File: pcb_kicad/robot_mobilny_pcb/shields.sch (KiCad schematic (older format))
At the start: 9 parts, among them J10 LIDAR, J11 MOTOR_1&2, J12 ENCODER_MOT_2, J13 ENCODER_MOT_3, J14 MOTOR_3&4, J15 ENCODER_MOT_4, J8 ENCODER_MOT_1, J9 UART_WIFI

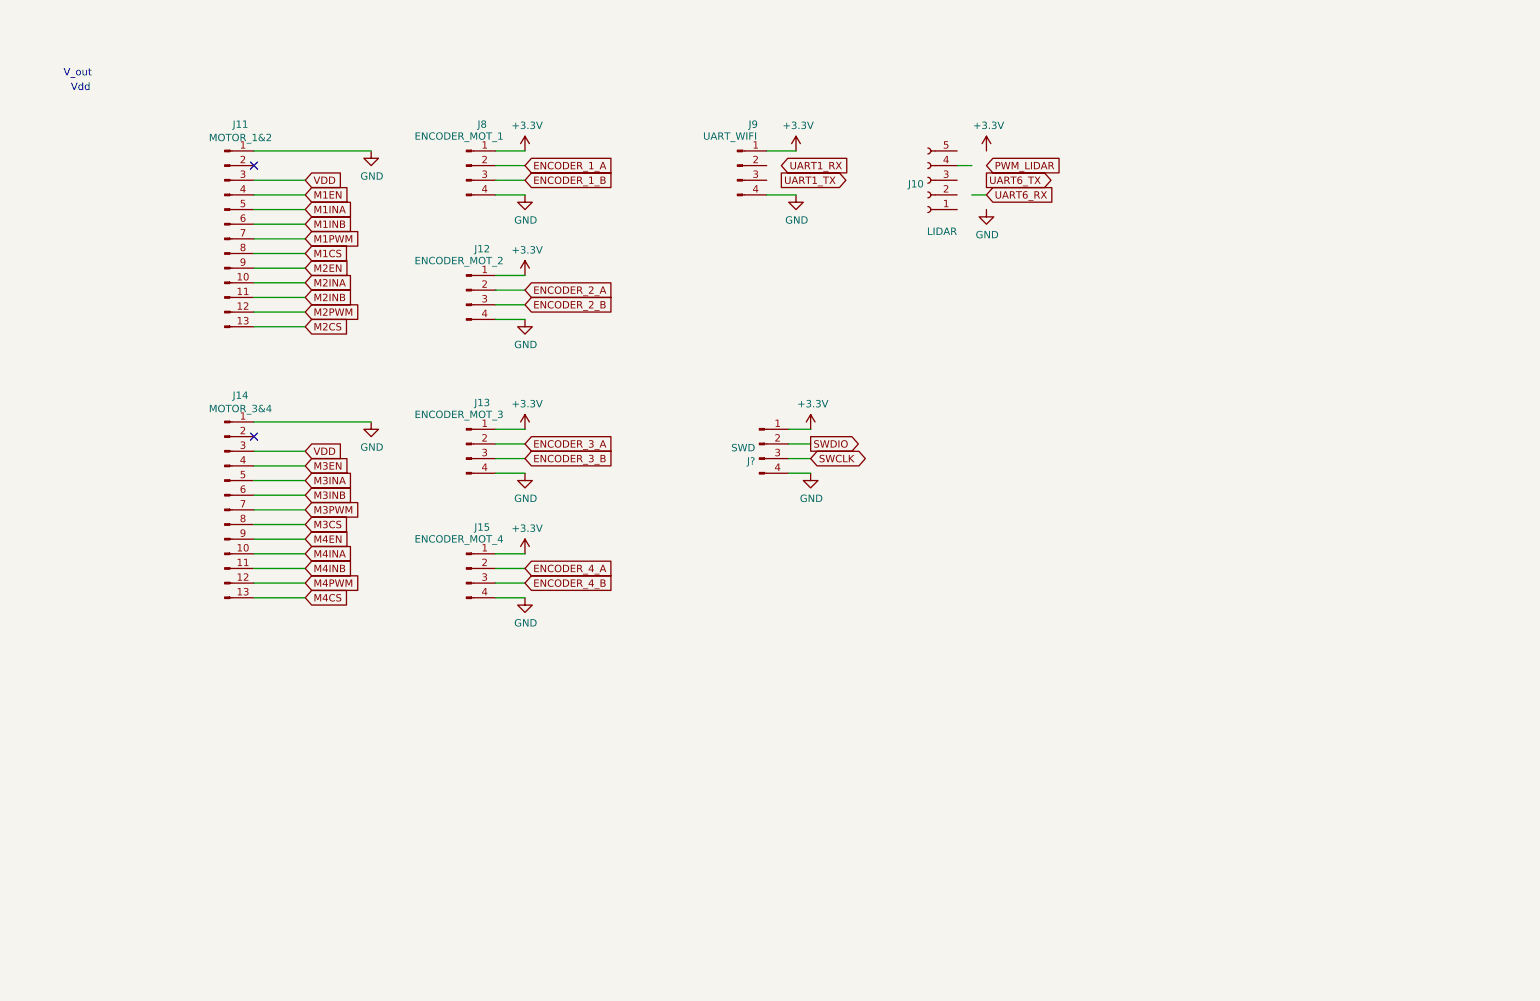
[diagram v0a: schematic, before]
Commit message: schematic update
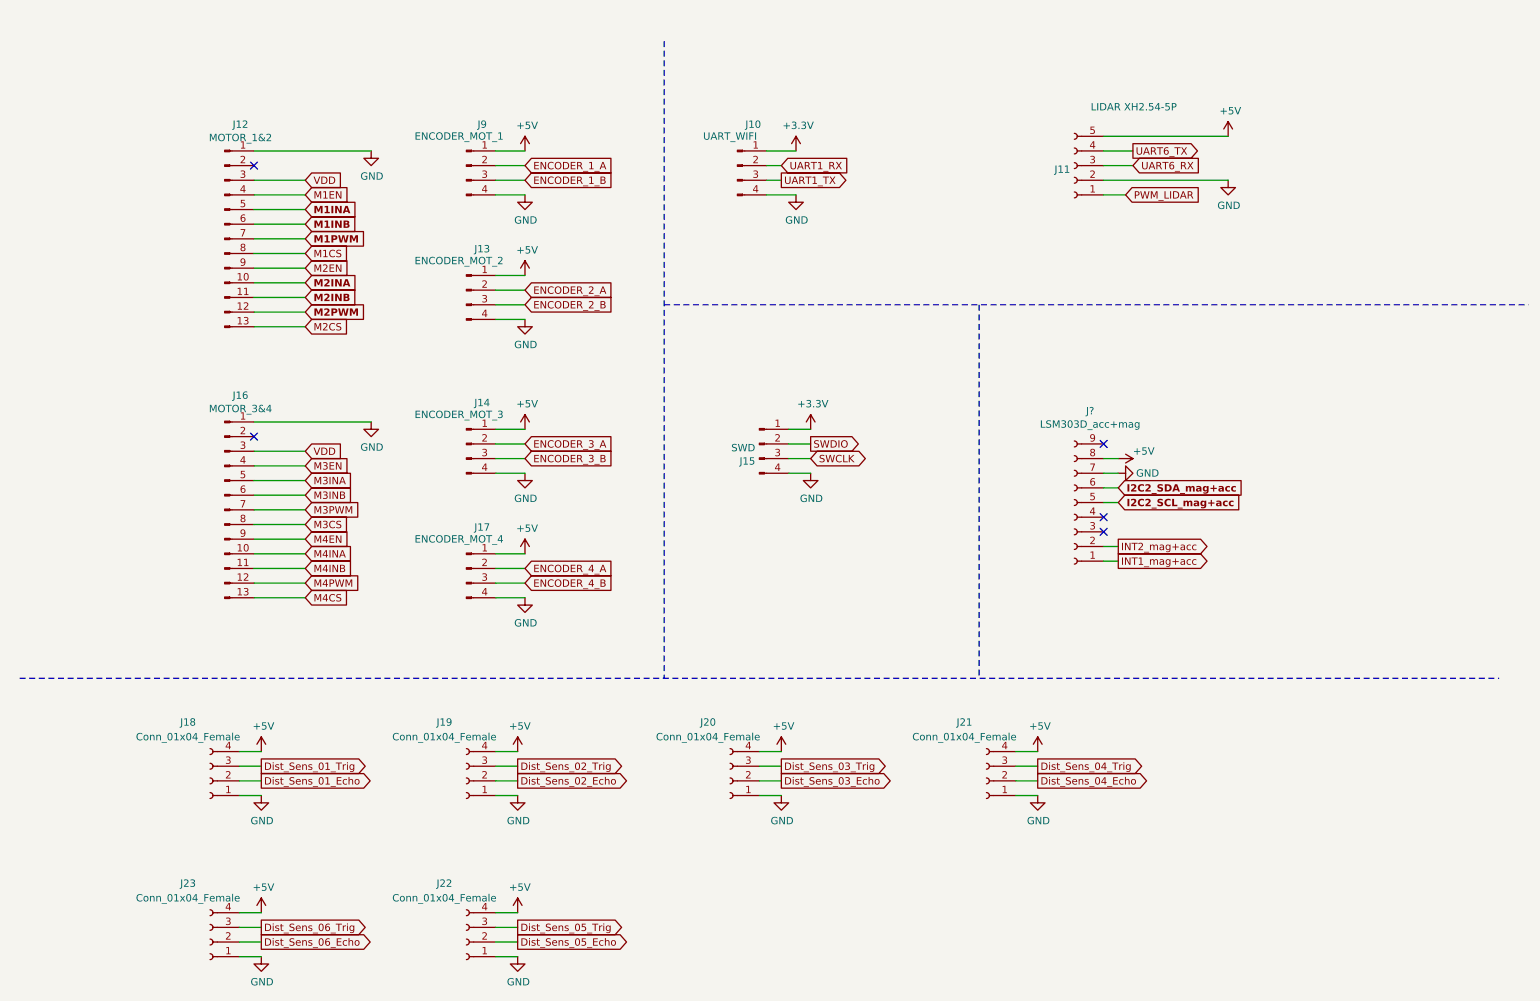
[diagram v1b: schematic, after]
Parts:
- added J18, J19, J20, J21, J22, J23: Conn_01x04_Female, Connector_PinSocket_2.54mm:PinSocket_1x04_P2.54mm_Vertical, symbol Connector:Conn_01x04_Female
- added J?: LSM303D_acc+mag, symbol Connector:Conn_01x09_Female
- J10: renamed from J9; footprint (none) -> Connector_Phoenix_MC_HighVoltage:PhoenixContact_MCV_1,5_4-G-5.08_1x04_P5.08mm_Vertical
- J11: renamed from J10; value LIDAR -> LIDAR XH2.54-5P; footprint (none) -> Connector_JST:JST_EH_B5B-EH-A_1x05_P2.50mm_Vertical
- J12: renamed from J11; footprint (none) -> Connector_PinHeader_2.54mm:PinHeader_1x13_P2.54mm_Vertical
- J13: renamed from J12; footprint (none) -> Connector_Phoenix_MC_HighVoltage:PhoenixContact_MCV_1,5_4-G-5.08_1x04_P5.08mm_Vertical
- J14: renamed from J13; footprint (none) -> Connector_Phoenix_MC_HighVoltage:PhoenixContact_MCV_1,5_4-G-5.08_1x04_P5.08mm_Vertical
- J15: renamed from J?; footprint (none) -> Connector_PinHeader_2.54mm:PinHeader_1x04_P2.54mm_Vertical
- J16: renamed from J14; footprint (none) -> Connector_PinHeader_2.54mm:PinHeader_1x13_P2.54mm_Vertical
- J17: renamed from J15; footprint (none) -> Connector_Phoenix_MC_HighVoltage:PhoenixContact_MCV_1,5_4-G-5.08_1x04_P5.08mm_Vertical
- J9: renamed from J8; footprint (none) -> Connector_Phoenix_MC_HighVoltage:PhoenixContact_MCV_1,5_4-G-5.08_1x04_P5.08mm_Vertical
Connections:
- net labels added: +5V, Dist_Sens_01_Echo, Dist_Sens_01_Trig, Dist_Sens_02_Echo, Dist_Sens_02_Trig, Dist_Sens_03_Echo, Dist_Sens_03_Trig, Dist_Sens_04_Echo, Dist_Sens_04_Trig, Dist_Sens_05_Echo, Dist_Sens_05_Trig, Dist_Sens_06_Echo, Dist_Sens_06_Trig, I2C2_SCL_mag+acc, I2C2_SDA_mag+acc, INT1_mag+acc, INT2_mag+acc
- wire segments 48 -> 83
- no-connect marks 2 -> 5
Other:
- note removed: "V_out"
- note removed: "Vdd\n"
- moved on the sheet: J11

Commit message: schematic_update
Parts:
- J308: renamed from J?; footprint (none) -> Connector_PinSocket_2.54mm:PinSocket_1x09_P2.54mm_Vertical
- J311: renamed from J18; footprint Connector_PinSocket_2.54mm:PinSocket_1x04_P2.54mm_Vertical -> Connector_PinHeader_2.54mm:PinHeader_1x04_P2.54mm_Vertical
- renumbered J9 to J301, J10 to J302, J11 to J303, J12 to J304, J13 to J305, J14 to J306, J15 to J307, J16 to J309, J17 to J310, J19 to J312, J20 to J313, J21 to J314, J23 to J315, J22 to J316
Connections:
- net M1EN is gone; now on net +3V3: J304.4 (Pin_4)
- net M2EN is gone; now on net +3V3: J304.9 (Pin_9)
- net M3EN is gone; now on net +3V3: J309.4 (Pin_4)
- net M4EN is gone; now on net +3V3: J309.9 (Pin_9)
- net M1CS: no longer names the net of J304.8 (Pin_8)
- net M2CS: no longer names the net of J304.13 (Pin_13)
- net M3CS: no longer names the net of J309.8 (Pin_8)
- net M4CS: no longer names the net of J309.13 (Pin_13)
- no-connect marks 5 -> 9

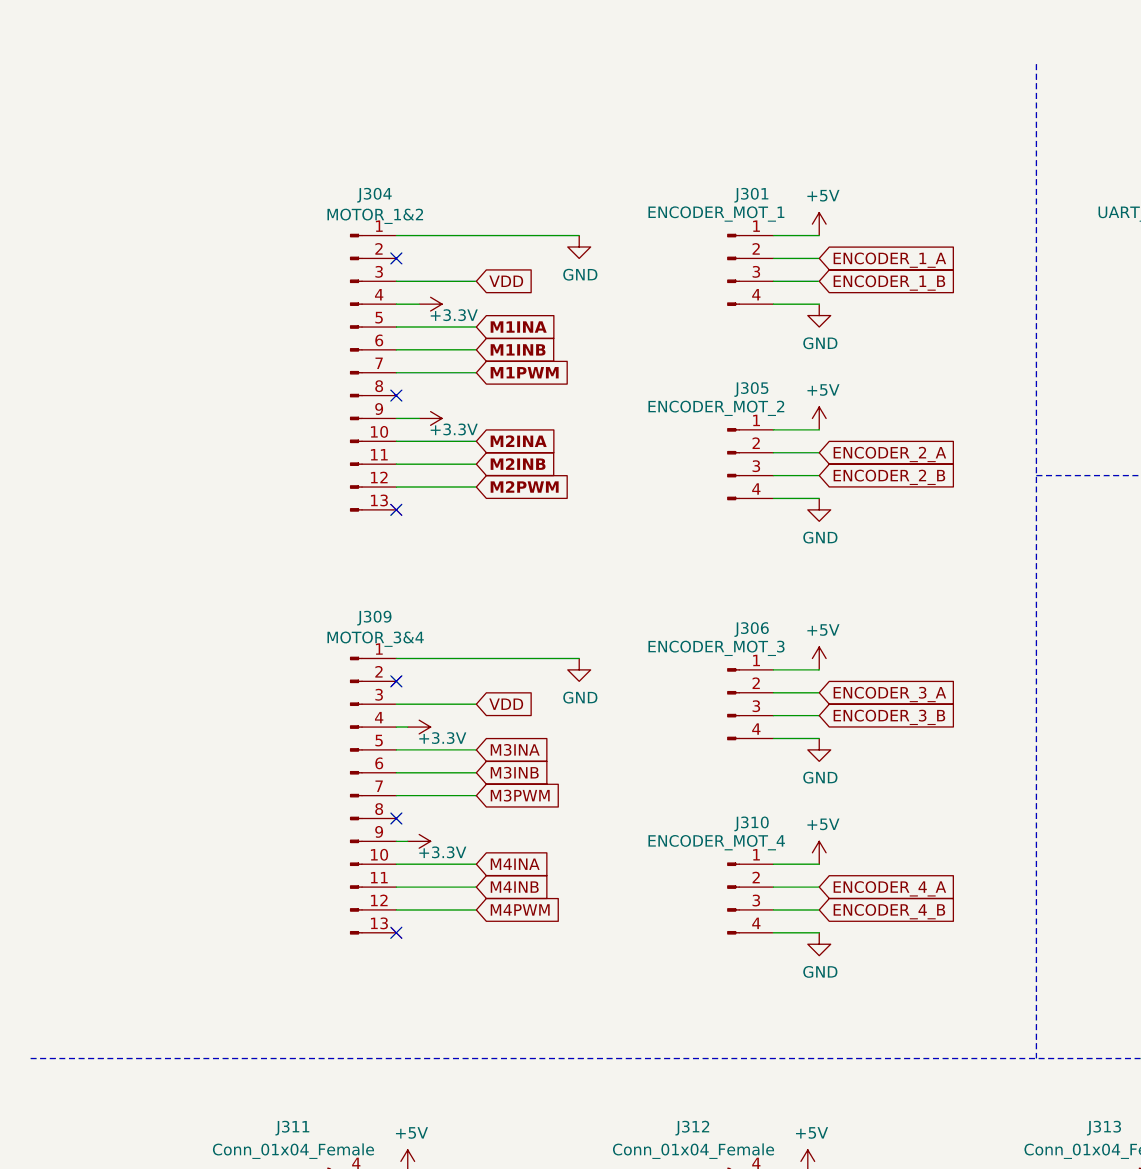
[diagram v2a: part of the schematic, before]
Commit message: PCB_update
Change of  motor controller connector to Arduino shields
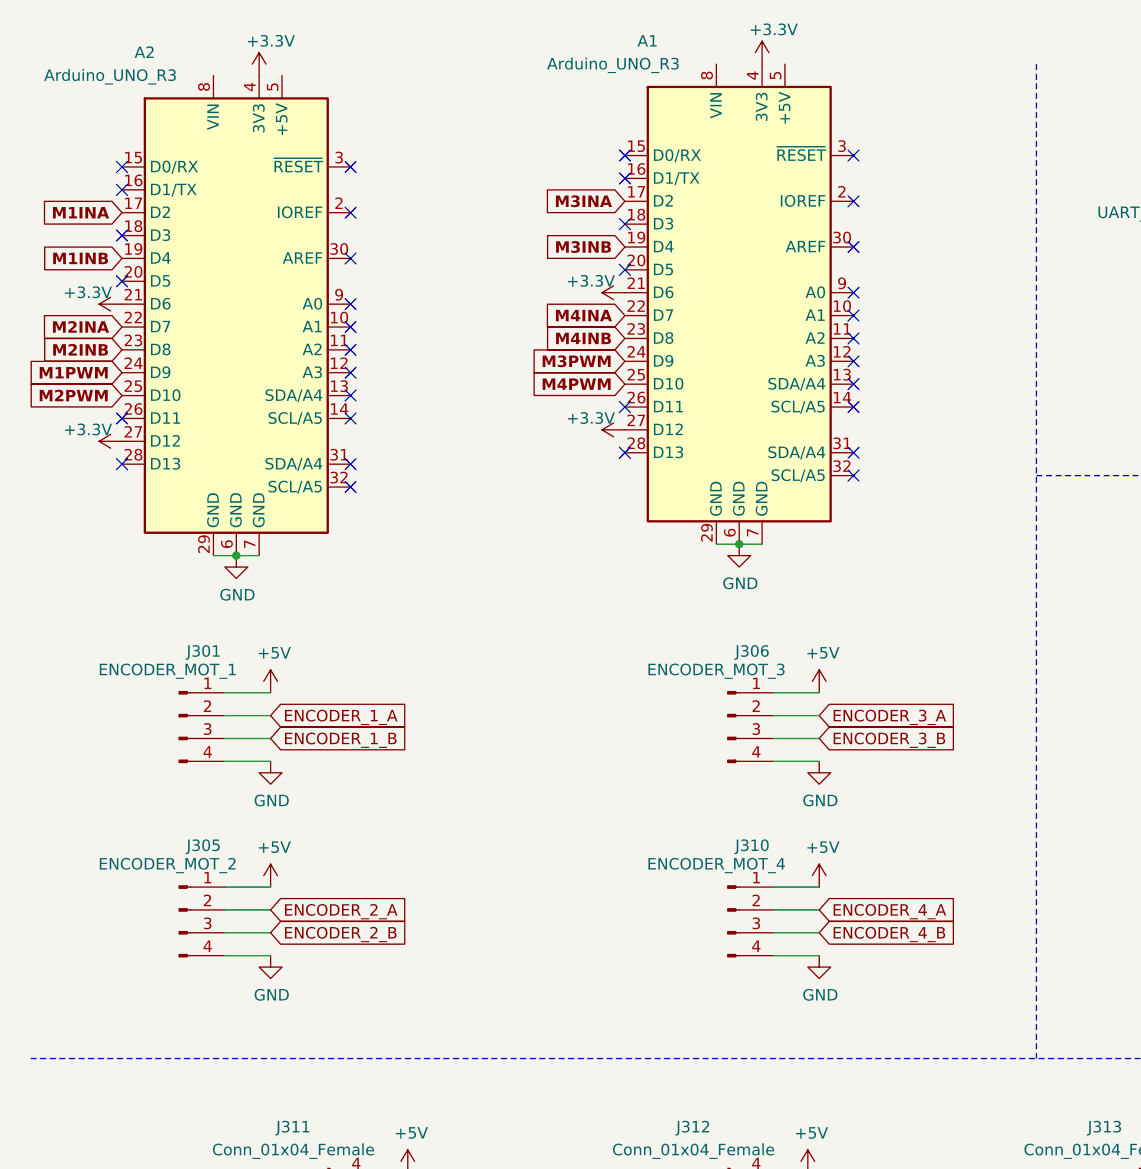
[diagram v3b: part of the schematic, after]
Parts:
- removed J304: MOTOR_1&2, Connector_PinHeader_2.54mm:PinHeader_1x13_P2.54mm_Vertical, symbol Connector:Conn_01x13_Male
- removed J309: MOTOR_3&4, Connector_PinHeader_2.54mm:PinHeader_1x13_P2.54mm_Vertical, symbol Connector:Conn_01x13_Male
- added A1, A2: Arduino_UNO_R3, Module:Arduino_UNO_R3, symbol MCU_Module:Arduino_UNO_R3
- J312: footprint Connector_PinSocket_2.54mm:PinSocket_1x04_P2.54mm_Vertical -> Connector_PinHeader_2.54mm:PinHeader_1x04_P2.54mm_Vertical
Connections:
- net +3V3: now also A1.21 (D6), A1.27 (D12), A1.4 (3V3), A2.21 (D6), A2.27 (D12), A2.4 (3V3)
- net GND: now also A1.29 (GND), A1.6 (GND), A1.7 (GND), A2.29 (GND), A2.6 (GND), A2.7 (GND)
- net M1INA: now also A2.17 (D2)
- net M1INB: now also A2.19 (D4)
- net M1PWM: now also A2.24 (D9)
- net M2INA: now also A2.22 (D7)
- net M2INB: now also A2.23 (D8)
- net M2PWM: now also A2.25 (D10)
- net M3INA: now also A1.17 (D2)
- net M3INB: now also A1.19 (D4)
- net M3PWM: now also A1.24 (D9)
- net M4INA: now also A1.22 (D7)
- net M4INB: now also A1.23 (D8)
- net M4PWM: now also A1.25 (D10)
- no-connect marks 9 -> 37
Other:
- moved on the sheet: J301, J305, J306, J310
